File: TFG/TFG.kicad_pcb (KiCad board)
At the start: 2 copper layers, 56.7 x 48.9 mm, 40 parts, among them IC1 MC74VHC1GT04DFT2G, IC2 TS1117BCW50 RPG, IC3 TS1117BCW50 RPG, J1 Jack-DC, J2 CON-SMA-EDGE-SRP, J3 CON-SMA-EDGE-SRP, Q1 BFP420

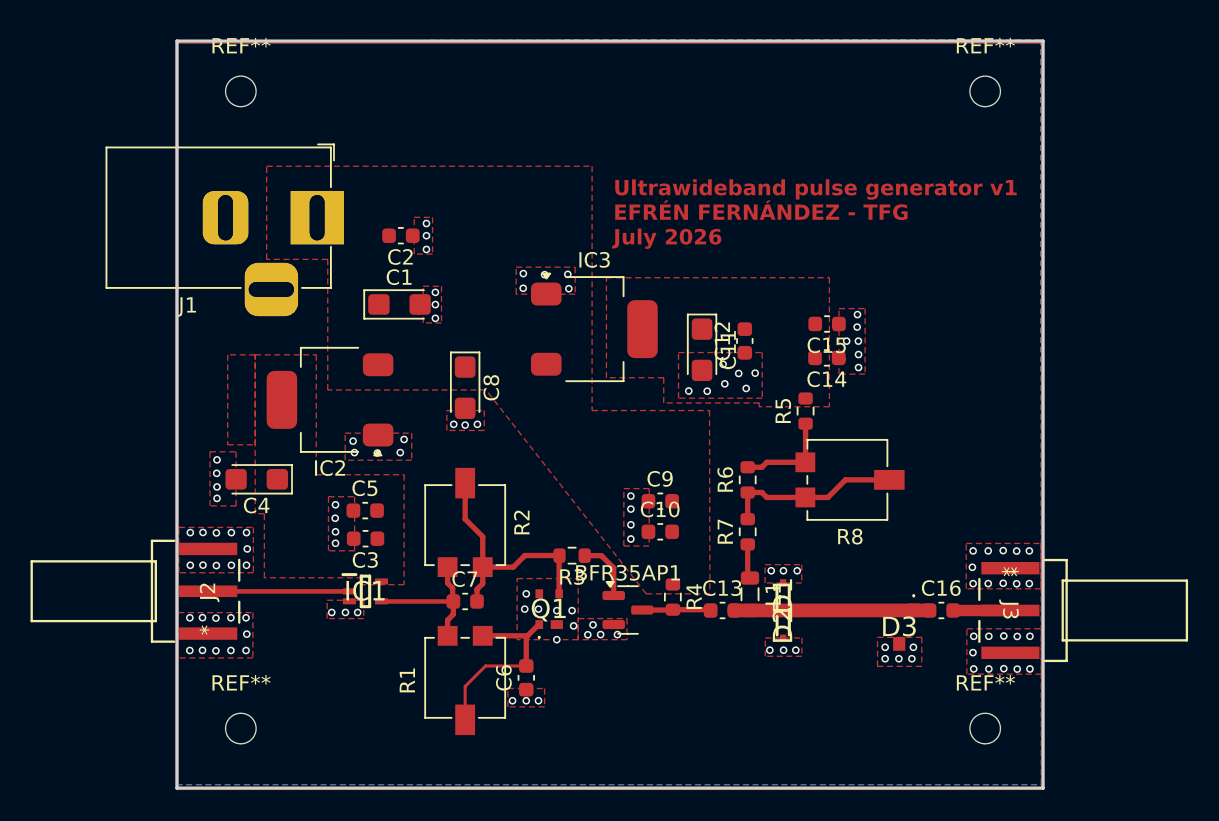
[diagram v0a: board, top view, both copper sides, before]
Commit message: Updated holes sizes to 0.5 mm and monospaced text
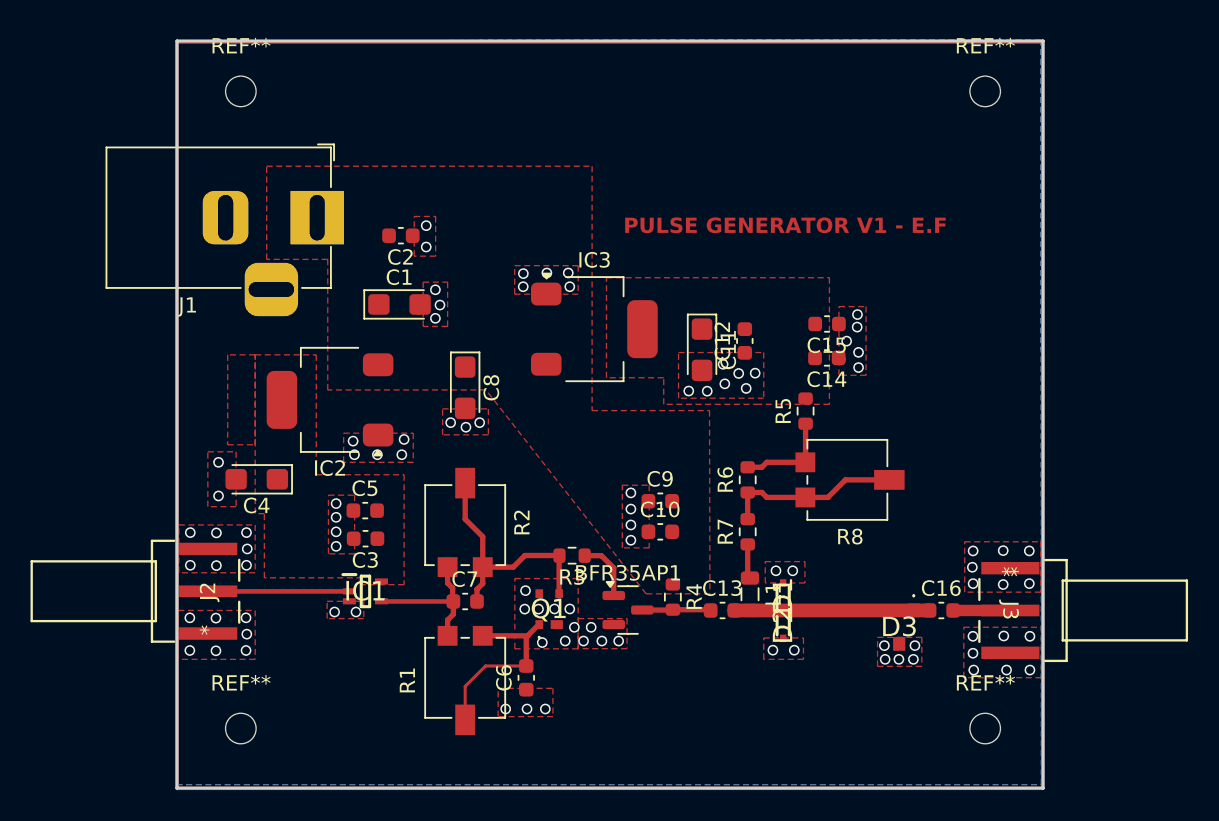
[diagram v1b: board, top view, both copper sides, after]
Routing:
- net GND: vias 116 -> 94
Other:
- board text added: "PULSE GENERATOR V1 - E.F"
- board text removed: "Ultrawideband pulse generator v1 EFRÉN FERNÁNDEZ - TFG July 2026"
